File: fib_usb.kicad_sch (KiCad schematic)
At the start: 137 parts, among them J401 USB-C_USB4105-GF-A, J402 Conn_USB-C_WE_632723300011, U3 TPS65988DHRSHR, U403 FT230X_QFN, U404 AP22615A_TSOT26, U405 TUSB1046-DCIRNQ, U406 AP22615A_TSOT26, U407 TPD4E05U06QDQARQ1, U408 TPD4E05U06QDQARQ1, U409 W25Q80DV_USON, U410 TPD4E05U06QDQARQ1, U411 TPD4E05U06QDQARQ1, U412 TPD4E05U06QDQARQ1

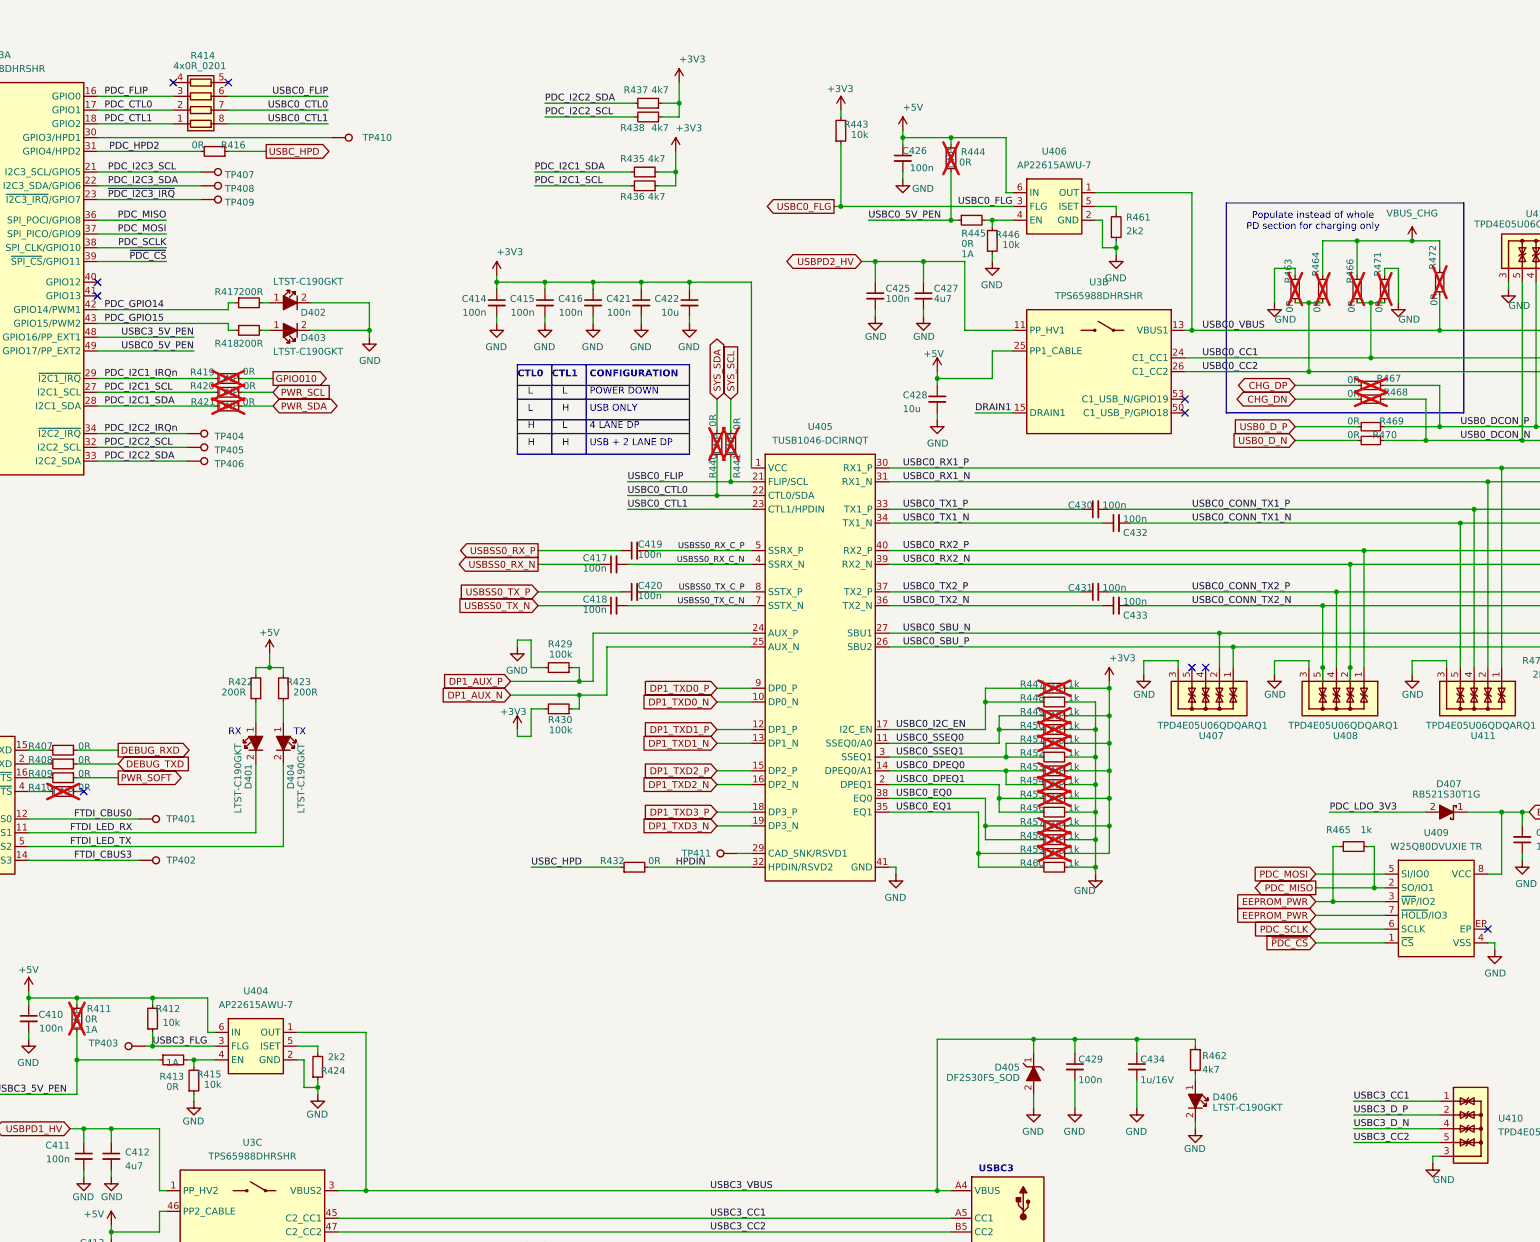
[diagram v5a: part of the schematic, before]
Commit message: implemented most of USB and Power Supplies
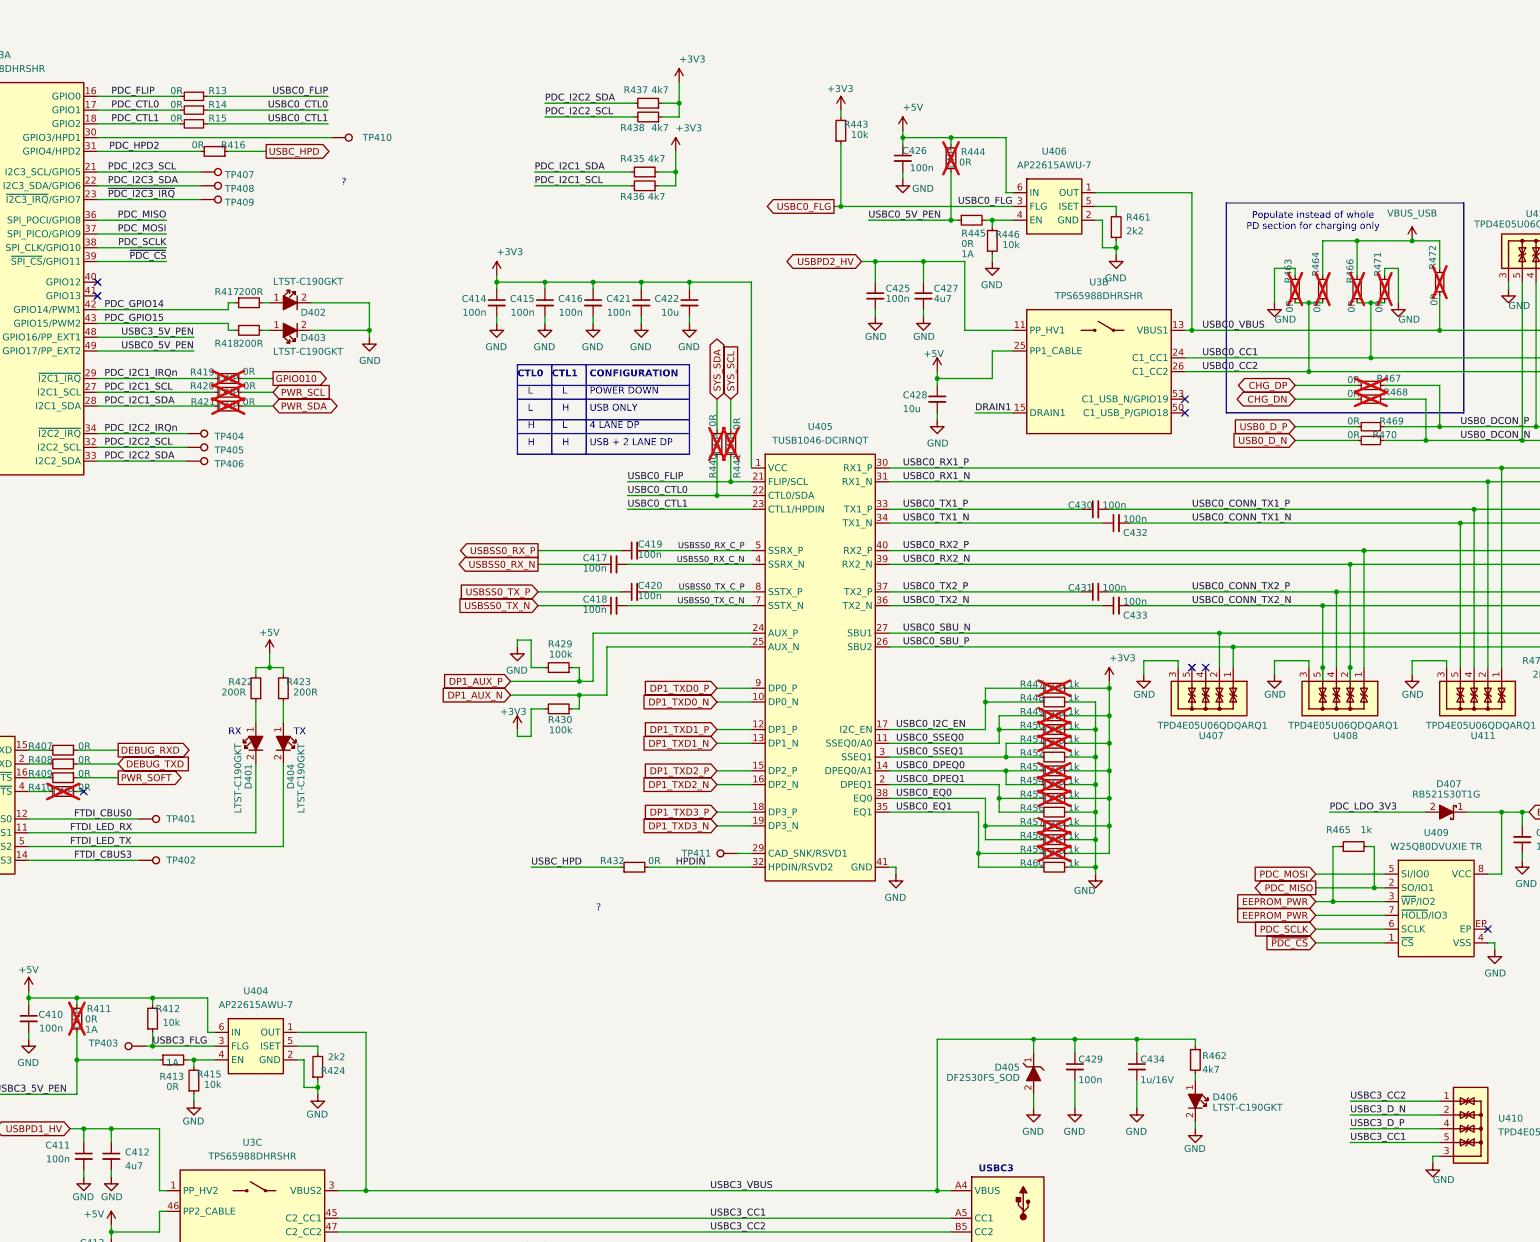
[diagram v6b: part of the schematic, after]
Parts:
- removed R414: R_4x0R_0201_array, jetson-orin-baseboard-footprints:R_Array_4x0201_Panasonic_EXB18V, symbol jetson-orin-baseboard:R_4x0R_0201_array
- added R13, R14, R15: 0R, Resistor_SMD:R_0402_1005Metric, symbol Device:R_Small
- C402, C407, C408, C409, C410, C411, C412, C423, C424, C425, C426, C427, C429, C435, C436: footprint Capacitor_SMD:C_0603_1608Metric -> Capacitor_SMD:C_0402_1005Metric
- C417, C418, C419, C420, C430, C431, C432, C433: footprint Capacitor_SMD:C_0201_0603Metric -> Capacitor_SMD:C_0402_1005Metric
- R401, R402, R403, R404, R405, R406, R407, R408, R409, R410, R411, R412, R413, R415, R416, R417, R418, R419, R420, R421, R422, R423, R424, R425, R426, R429, R430, R432, R435, R436, R437, R438, R440, R441, R443, R444, R445, R446, R461, R462, R463, R464, R465, R466, R467, R468, R471, R473, R474, R475: footprint Resistor_SMD:R_0603_1608Metric -> Resistor_SMD:R_0402_1005Metric
- TP401, TP402, TP403, TP404, TP405, TP406, TP407, TP408, TP409, TP410, TP411: footprint TestPoint:TestPoint_Pad_D1.0mm -> (none)
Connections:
- net PDC_CTL0: now also R14.2
- net PDC_CTL1: now also R15.2
- net PDC_FLIP: now also R13.2
- net USBC0_CTL0: now also R14.1
- net USBC0_CTL1: now also R15.1
- net USBC0_FLIP: now also R13.1
- net USBC3_CC1: now also U410.5, U410.6; no longer U410.1, U410.10
- net USBC3_CC2: now also U410.1, U410.10; no longer U410.5, U410.6
- net USBC3_D_N: now also U410.2, U410.9; no longer U410.4, U410.7
- net USBC3_D_P: now also U410.4, U410.7; no longer U410.2, U410.9
- net VBUS_CHG renamed VBUS_USB
- no-connect marks 14 -> 12
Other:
- note added: "?"

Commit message: further optimized placement, finished most of buck array, expanded pcie, added tons of missing footprints, diff pair spacing optimization
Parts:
- D401, D402, D403, D404, D406, D409: footprint jetson-orin-baseboard-footprints:LED_0603_1608Metric_G -> LED_SMD:LED_0603_1608Metric
- D405, D408: footprint jetson-orin-baseboard-footprints:SOD-923 -> Diode_SMD:D_SOD-923
- D407: footprint jetson-orin-baseboard-footprints:SOD-523 -> Diode_SMD:D_SOD-523
- TP401, TP402, TP403, TP404, TP405, TP406, TP407, TP408, TP409, TP410, TP411: footprint (none) -> TestPoint:TestPoint_Pad_D1.0mm
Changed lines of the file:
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@@
 			)
 		)
-		(property "Footprint" "jetson-orin-baseboard-footprints:SOD-923"
+		(property "Footprint" "Diode_SMD:D_SOD-923"
 			(at 273.05 193.04 0)
 			(effects
@@
 			)
 		)
-		(property "Footprint" "jetson-orin-baseboard-footprints:LED_0603_1608Metric_G"
+		(property "Footprint" "LED_SMD:LED_0603_1608Metric"
 			(at 285.115 234.95 0)
 			(effects
@@
 			)
 		)
-		(property "Footprint" ""
+		(property "Footprint" "TestPoint:TestPoint_Pad_D1.0mm"
 			(at 127 59.69 0)
 			(effects
@@
 			)
 		)
-		(property "Footprint" "jetson-orin-baseboard-footprints:LED_0603_1608Metric_G"
+		(property "Footprint" "LED_SMD:LED_0603_1608Metric"
 			(at 147.32 78.74 0)
 			(effects
@@
 			)
 		)
-		(property "Footprint" ""
+		(property "Footprint" "TestPoint:TestPoint_Pad_D1.0mm"
 			(at 195.58 160.02 0)
 			(effects
@@
 			)
 		)
-		(property "Footprint" "jetson-orin-baseboard-footprints:LED_0603_1608Metric_G"
+		(property "Footprint" "LED_SMD:LED_0603_1608Metric"
 			(at 147.32 63.5 0)
 			(effects
@@
 			)
 		)
-		(property "Footprint" ""
+		(property "Footprint" "TestPoint:TestPoint_Pad_D1.0mm"
 			(at 127 57.15 0)
 			(effects
@@
 			)
 		)
-		(property "Footprint" "jetson-orin-baseboard-footprints:LED_0603_1608Metric_G"
+		(property "Footprint" "LED_SMD:LED_0603_1608Metric"
 			(at 132.08 168.91 0)
 			(effects
@@
 			)
 		)
-		(property "Footprint" ""
+		(property "Footprint" "TestPoint:TestPoint_Pad_D1.0mm"
 			(at 124.46 105.41 0)
 			(effects
@@
 			)
 		)
-		(property "Footprint" "jetson-orin-baseboard-footprints:SOD-523"
+		(property "Footprint" "Diode_SMD:D_SOD-523"
 			(at 360.68 172.72 0)
 			(effects
@@
 			)
 		)
-		(property "Footprint" ""
+		(property "Footprint" "TestPoint:TestPoint_Pad_D1.0mm"
 			(at 127 54.61 0)
 			(effects
@@
 			)
 		)
-		(property "Footprint" ""
+		(property "Footprint" "TestPoint:TestPoint_Pad_D1.0mm"
 			(at 86.36 195.58 0)
 			(effects
@@
 			)
 		)
-		(property "Footprint" ""
+		(property "Footprint" "TestPoint:TestPoint_Pad_D1.0mm"
 			(at 151.13 48.26 0)
 			(effects
@@
 			)
 		)
-		(property "Footprint" "jetson-orin-baseboard-footprints:LED_0603_1608Metric_G"
+		(property "Footprint" "LED_SMD:LED_0603_1608Metric"
 			(at 116.84 168.91 0)
 			(effects
@@
 			)
 		)
-		(property "Footprint" ""
+		(property "Footprint" "TestPoint:TestPoint_Pad_D1.0mm"
 			(at 115.57 181.61 0)
 			(effects
@@
 			)
 		)
-		(property "Footprint" "jetson-orin-baseboard-footprints:LED_0603_1608Metric_G"
+		(property "Footprint" "LED_SMD:LED_0603_1608Metric"
 			(at 387.35 73.66 0)
 			(effects
@@
 			)
 		)
-		(property "Footprint" ""
+		(property "Footprint" "TestPoint:TestPoint_Pad_D1.0mm"
 			(at 115.57 173.99 0)
 			(effects
@@
 			)
 		)
-		(property "Footprint" ""
+		(property "Footprint" "TestPoint:TestPoint_Pad_D1.0mm"
 			(at 124.46 102.87 0)
 			(effects
@@
 			)
 		)
-		(property "Footprint" ""
+		(property "Footprint" "TestPoint:TestPoint_Pad_D1.0mm"
 			(at 124.46 107.95 0)
 			(effects
@@
 			)
 		)
-		(property "Footprint" "jetson-orin-baseboard-footprints:SOD-923"
+		(property "Footprint" "Diode_SMD:D_SOD-923"
 			(at 381 29.21 0)
 			(effects

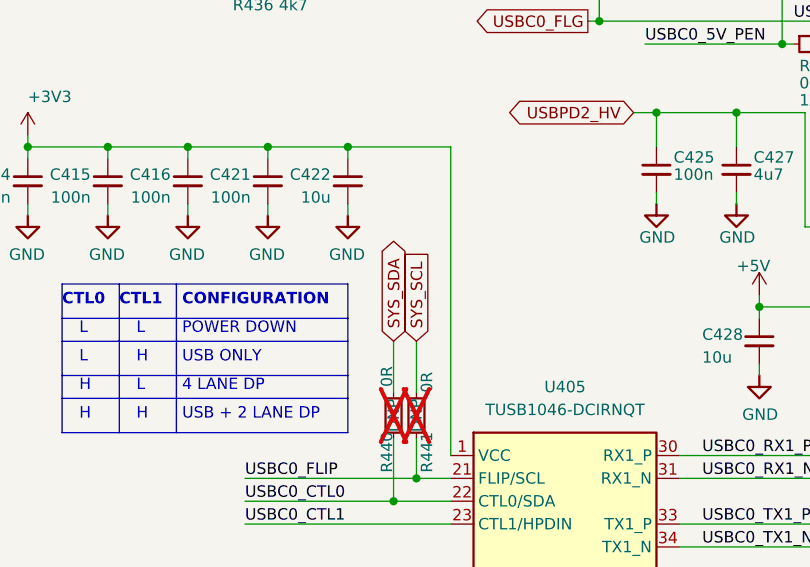
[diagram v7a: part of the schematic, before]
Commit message: 90 percent done with routing. need to go over all schematic pages, double check everything thoroughly, do lengthmatching add any missing footprints, take care of startup, ferrites, audio, eink connectors, 40pin header connections, rtc
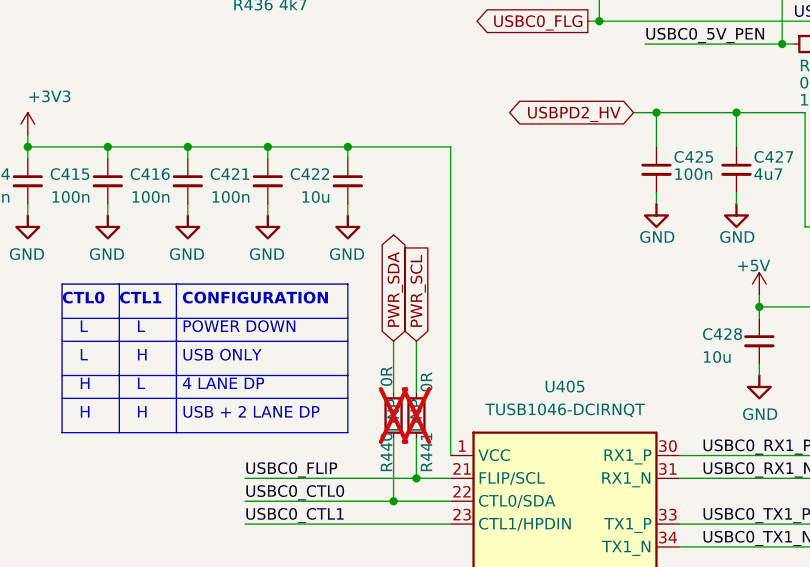
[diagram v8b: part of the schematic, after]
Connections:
- net SYS_SCL is gone; now on net PWR_SCL: R441.2
- net SYS_SDA is gone; now on net PWR_SDA: R440.2
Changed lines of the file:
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@@
 		)
 	)
-	(global_label "SYS_SDA"
+	(global_label "PWR_SDA"
 		(shape bidirectional)
 		(at 207.01 86.36 90)
@@
 		)
 	)
-	(global_label "SYS_SCL"
+	(global_label "PWR_SCL"
 		(shape input)
 		(at 209.55 86.36 90)
